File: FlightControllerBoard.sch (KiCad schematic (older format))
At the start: 18 parts, among them J1 Conn_01x02, J10 Conn_01x02, J11 Conn_01x02, J12 Conn_01x03_Male, J2 Conn_01x03_Male, J3 Conn_01x03_Male, J4 Conn_01x03_Male, J5 Conn_01x03_Male, J6 Conn_01x03_Male, J7 Conn_01x03_Male, J8 Conn_01x03_Male, J9 Conn_01x03_Male, Q1 BSS138

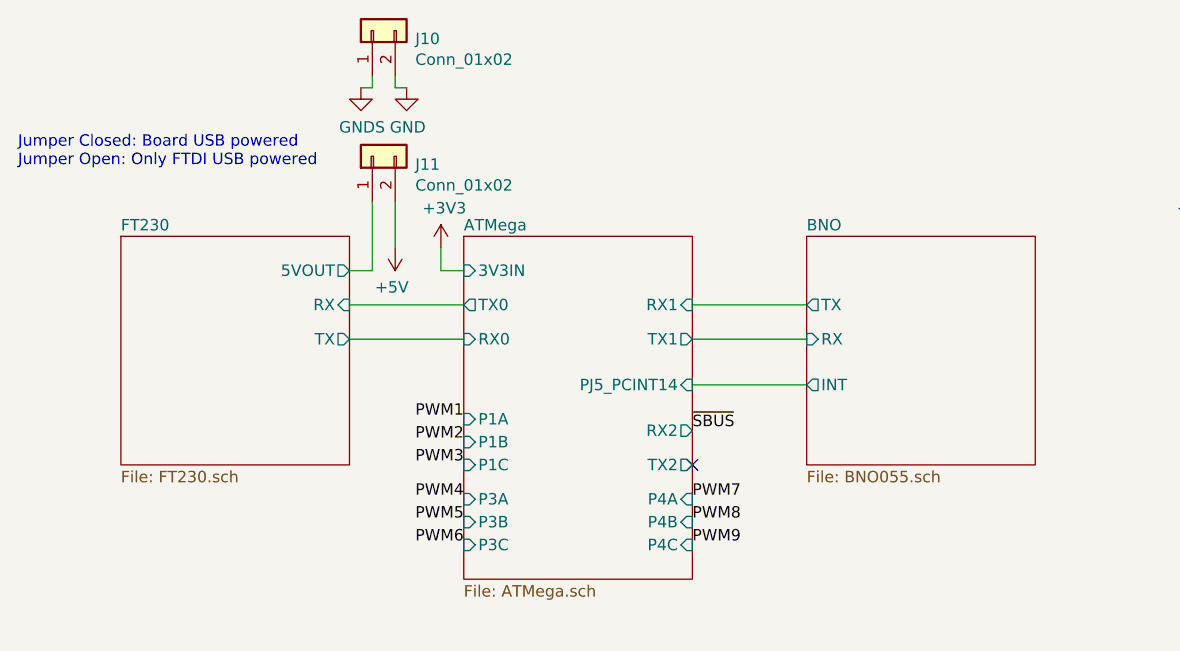
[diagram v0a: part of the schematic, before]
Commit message: use submodule for FT230
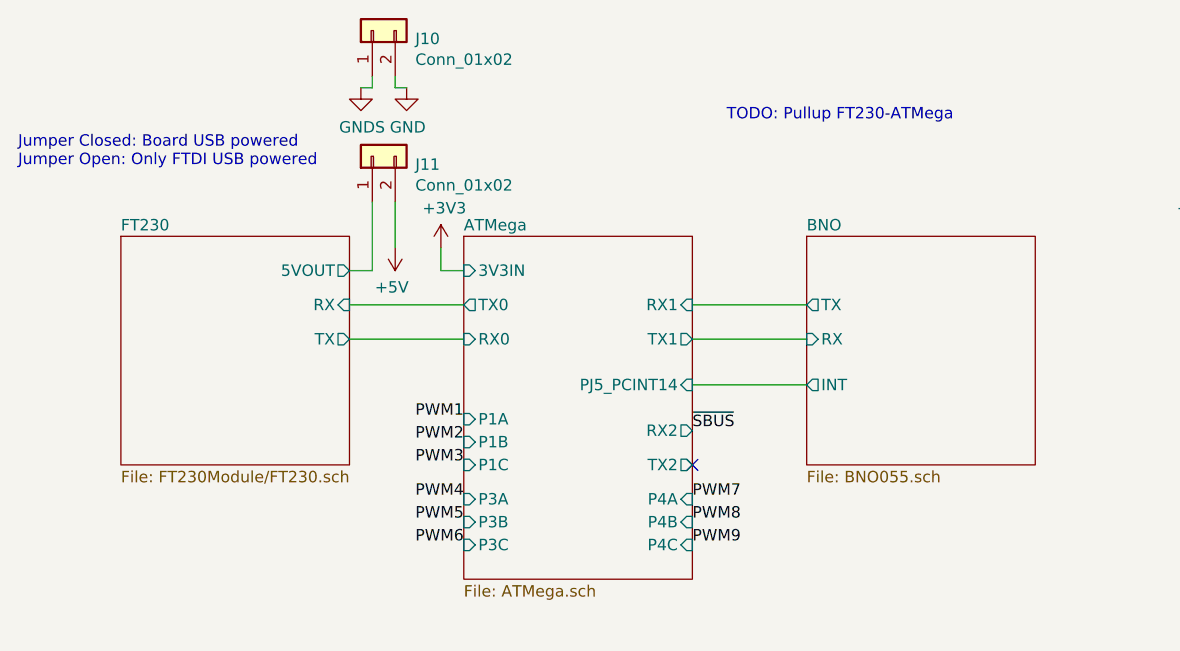
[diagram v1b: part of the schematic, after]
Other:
- note added: "TODO: Pullup FT230-ATMega"
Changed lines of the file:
@@
 U 5C901AA2
 F0 "FT230" 50
-F1 "FT230.sch" 50
+F1 "FT230Module/FT230.sch" 50
 F2 "TX" O R 2000 1950 50
 F3 "RX" I R 2000 1800 50
@@
 Wire Wire Line
 	2200 850  2250 850
+Text Notes 3650 1000 0    50   ~ 0
+TODO: Pullup FT230-ATMega
 $EndSCHEMATC

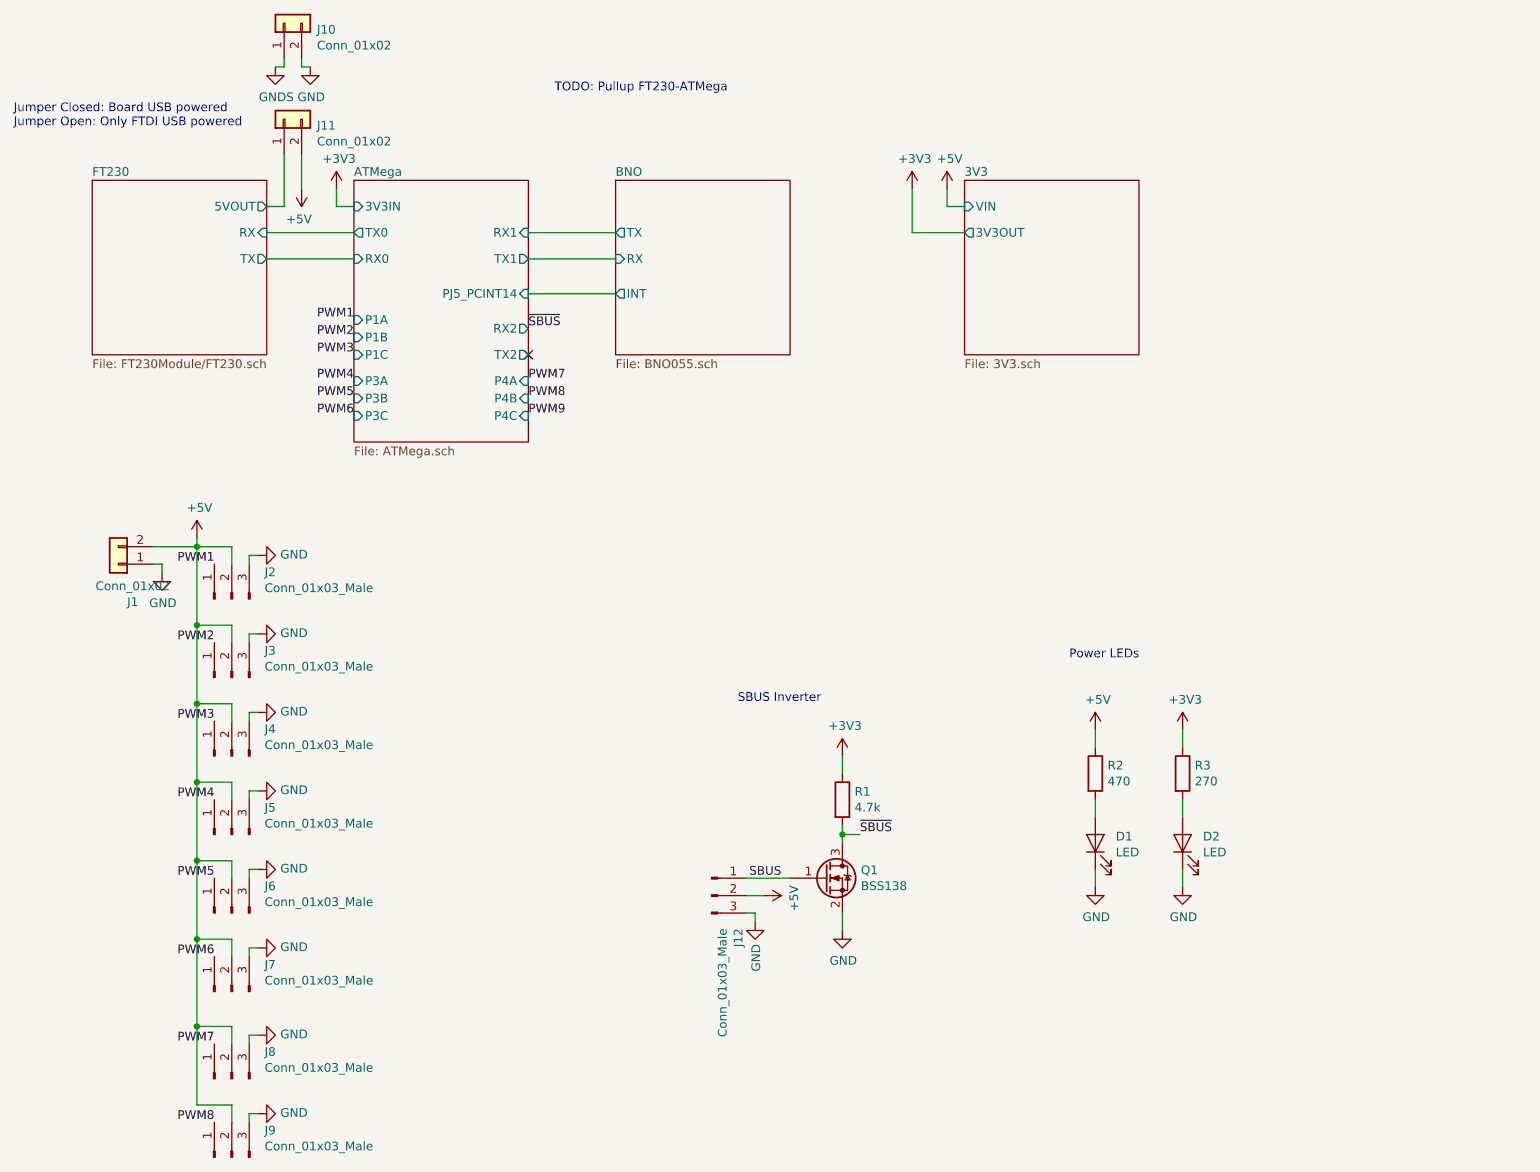
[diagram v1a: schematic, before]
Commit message: pullups, jumpers
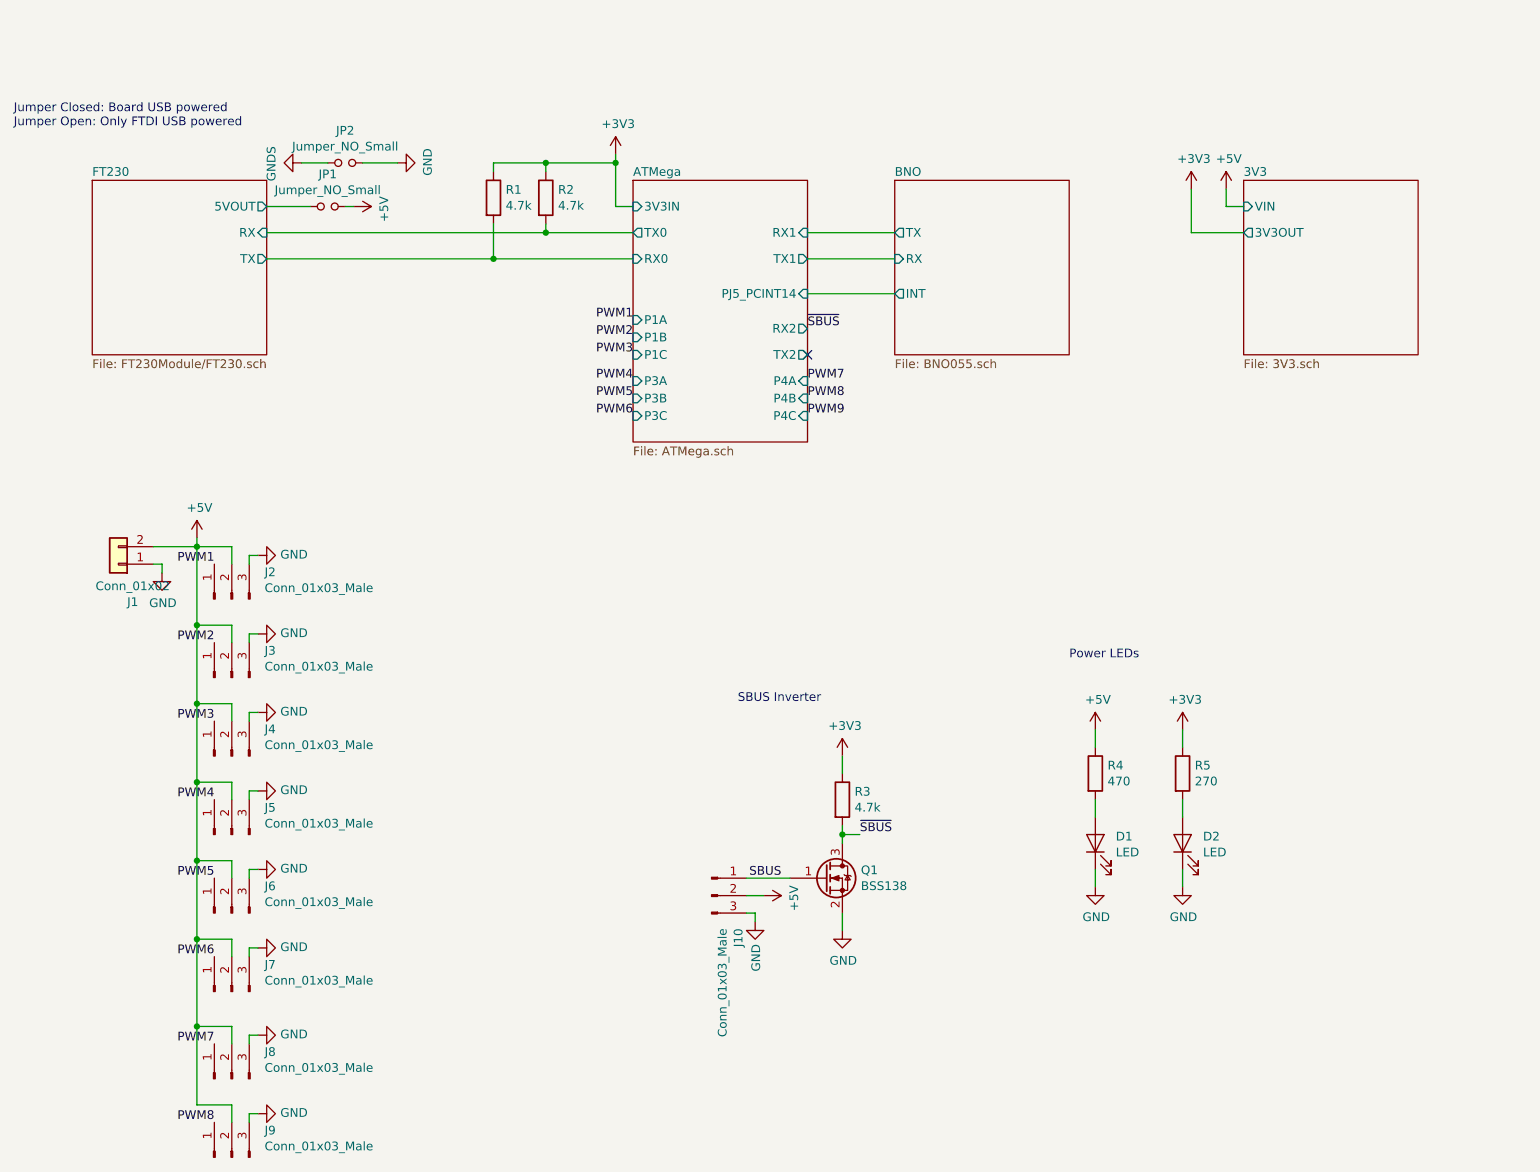
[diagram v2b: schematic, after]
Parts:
- removed J10, J11: Conn_01x02, Connector_PinHeader_2.54mm:PinHeader_1x02_P2.54mm_Vertical, symbol Connector_Generic:Conn_01x02
- added JP1, JP2: Jumper_NO_Small, Connector_PinHeader_2.54mm:PinHeader_1x02_P2.54mm_Vertical, symbol Device:Jumper_NO_Small
- added R1, R2: 4.7k, Resistor_SMD:R_0603_1608Metric, symbol Device:R
- renumbered J12 to J10, R1 to R3, R2 to R4, R3 to R5
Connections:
- net +3V3: now also R1.1, R2.1
- net +5V: now also JP1.2
- net ATMega/RX0: now also R1.2
- net ATMega/TX0: now also R2.2
- net FT230/5VOUT: now also JP1.1
- net GND: now also JP2.2
- net GNDS: now also JP2.1
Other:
- note removed: "TODO: Pullup FT230-ATMega"

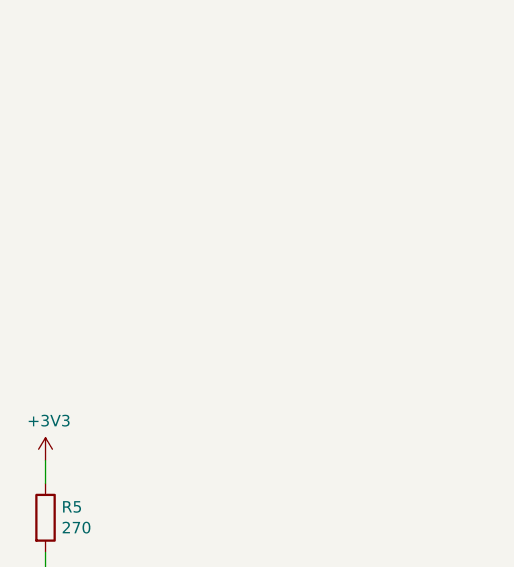
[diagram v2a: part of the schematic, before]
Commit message: LED, Mounting Holes
LEDs to register L
Mounting Holes
XT30
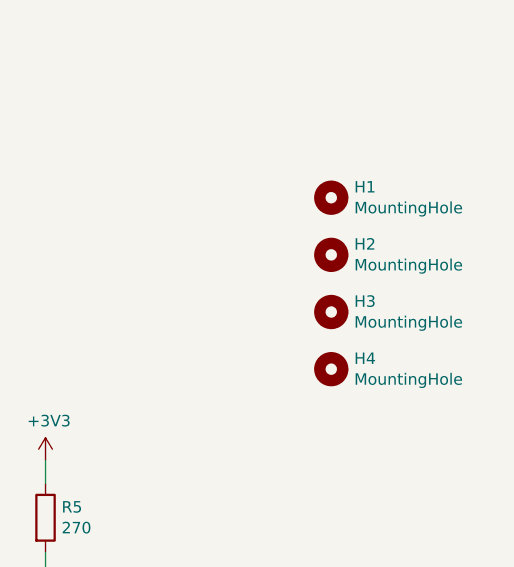
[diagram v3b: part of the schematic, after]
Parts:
- added H1, H2, H3, H4: MountingHole, MountingHole:MountingHole_3.2mm_M3, symbol Mechanical:MountingHole
- J1: footprint XT30:XT30PB-M -> Connector_AMASS:AMASS_XT30UPB-M_1x02_P5.0mm_Vertical
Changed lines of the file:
@@
 F 0 "J1" H 1068 3917 50  0000 C CNN
 F 1 "Conn_01x02" H 1068 3826 50  0000 C CNN
-F 2 "XT30:XT30PB-M" H 1150 3700 50  0001 C CNN
+F 2 "Connector_AMASS:AMASS_XT30UPB-M_1x02_P5.0mm_Vertical" H 1150 3700 50  0001 C CNN
 F 3 "~" H 1150 3700 50  0001 C CNN
 	1    1150 3700
@@
 Wire Wire Line
 	2500 1650 2450 1650
+$Comp
+L Mechanical:MountingHole H1
+U 1 1 5CA9C4CA
+P 8500 3500
+F 0 "H1" H 8600 3546 50  0000 L CNN
+F 1 "MountingHole" H 8600 3455 50  0000 L CNN
+F 2 "MountingHole:MountingHole_3.2mm_M3" H 8500 3500 50  0001 C CNN
+F 3 "~" H 8500 3500 50  0001 C CNN
+	1    8500 3500
+	1    0    0    -1
+$EndComp
+$Comp
+L Mechanical:MountingHole H2
+U 1 1 5CA9C92B
+P 8500 3750
+F 0 "H2" H 8600 3796 50  0000 L CNN
+F 1 "MountingHole" H 8600 3705 50  0000 L CNN
+F 2 "MountingHole:MountingHole_3.2mm_M3" H 8500 3750 50  0001 C CNN
+F 3 "~" H 8500 3750 50  0001 C CNN
+	1    8500 3750
+	1    0    0    -1
+$EndComp
+$Comp
+L Mechanical:MountingHole H3
+U 1 1 5CA9CB68
+P 8500 4000
+F 0 "H3" H 8600 4046 50  0000 L CNN
+F 1 "MountingHole" H 8600 3955 50  0000 L CNN
+F 2 "MountingHole:MountingHole_3.2mm_M3" H 8500 4000 50  0001 C CNN
+F 3 "~" H 8500 4000 50  0001 C CNN
+	1    8500 4000
+	1    0    0    -1
+$EndComp
+$Comp
+L Mechanical:MountingHole H4
+U 1 1 5CA9CE24
+P 8500 4250
+F 0 "H4" H 8600 4296 50  0000 L CNN
+F 1 "MountingHole" H 8600 4205 50  0000 L CNN
+F 2 "MountingHole:MountingHole_3.2mm_M3" H 8500 4250 50  0001 C CNN
+F 3 "~" H 8500 4250 50  0001 C CNN
+	1    8500 4250
+	1    0    0    -1
+$EndComp
 $EndSCHEMATC

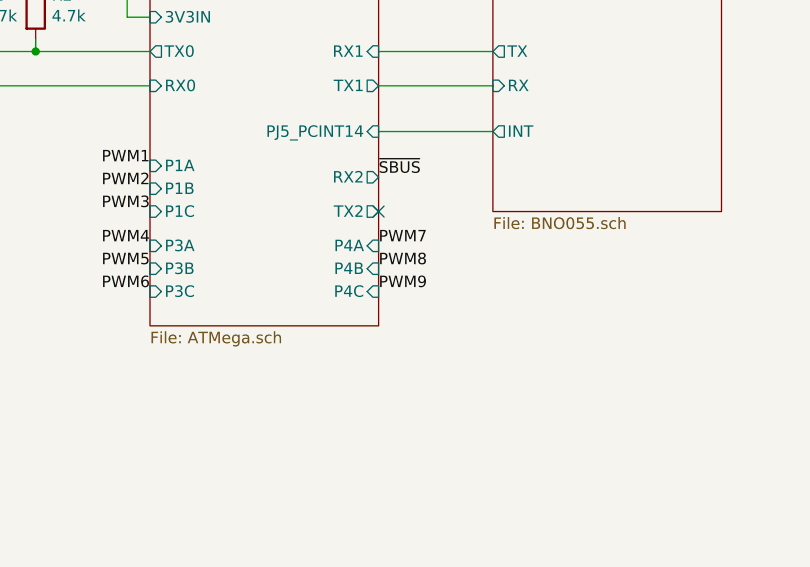
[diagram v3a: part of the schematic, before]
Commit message: added NCs to satisfy ERC
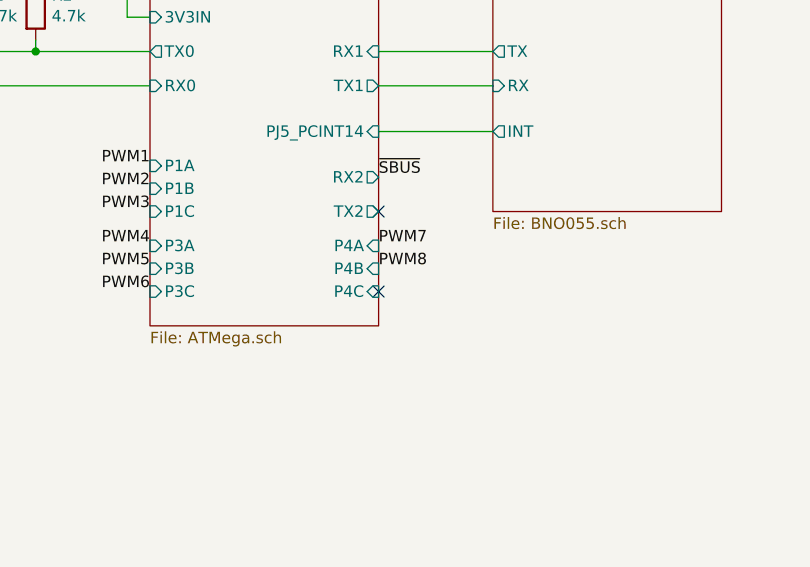
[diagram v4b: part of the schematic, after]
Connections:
- no-connect marks 1 -> 2
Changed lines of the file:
@@
 Text Label 5100 2750 0    50   ~ 0
 PWM8
-Text Label 5100 2850 0    50   ~ 0
-PWM9
 Text Label 1700 3700 2    50   ~ 0
 PWM1
@@
 	1    0    0    -1
 $EndComp
+NoConn ~ 5100 2850
 $EndSCHEMATC
